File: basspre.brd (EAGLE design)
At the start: 41.3 x 28.7 mm, 27 parts, among them U1 LM4250, U101 TLE2426IDR, U103 LM4250

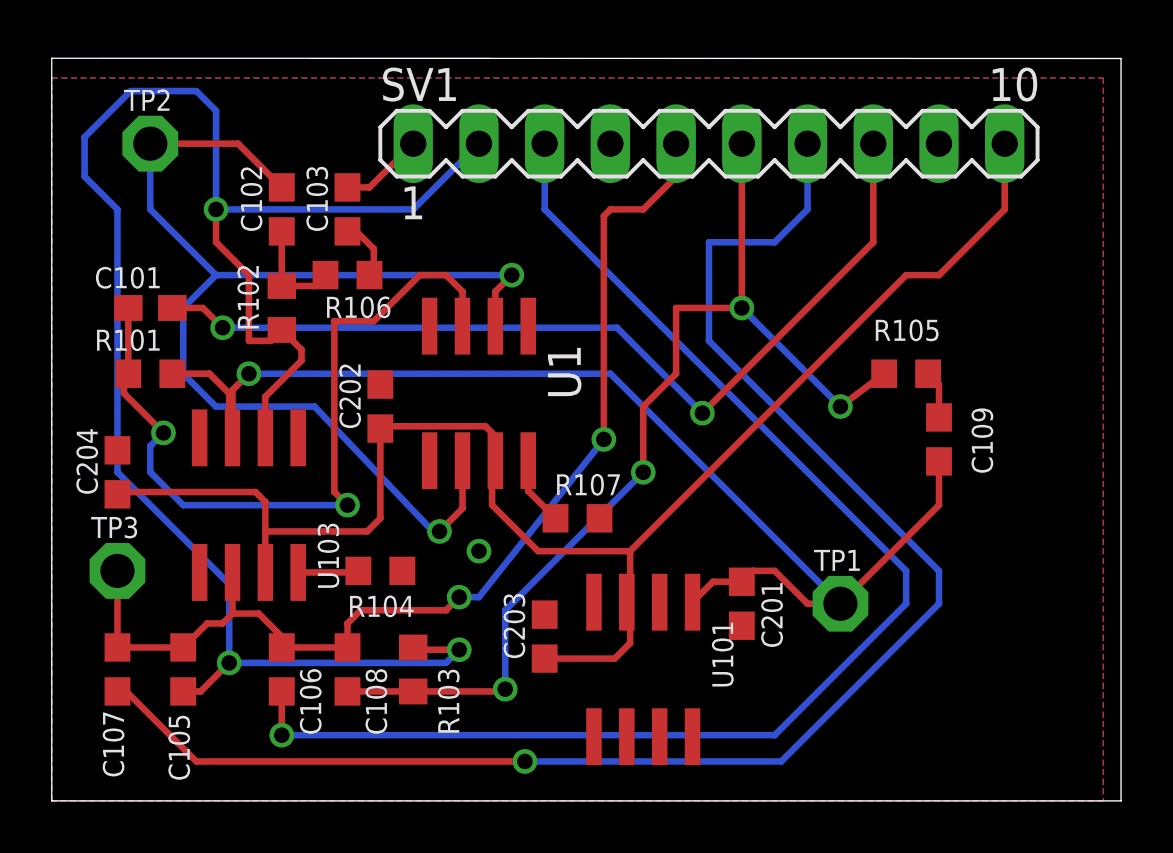
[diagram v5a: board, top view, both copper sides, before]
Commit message: changed bypass caps to 0805.
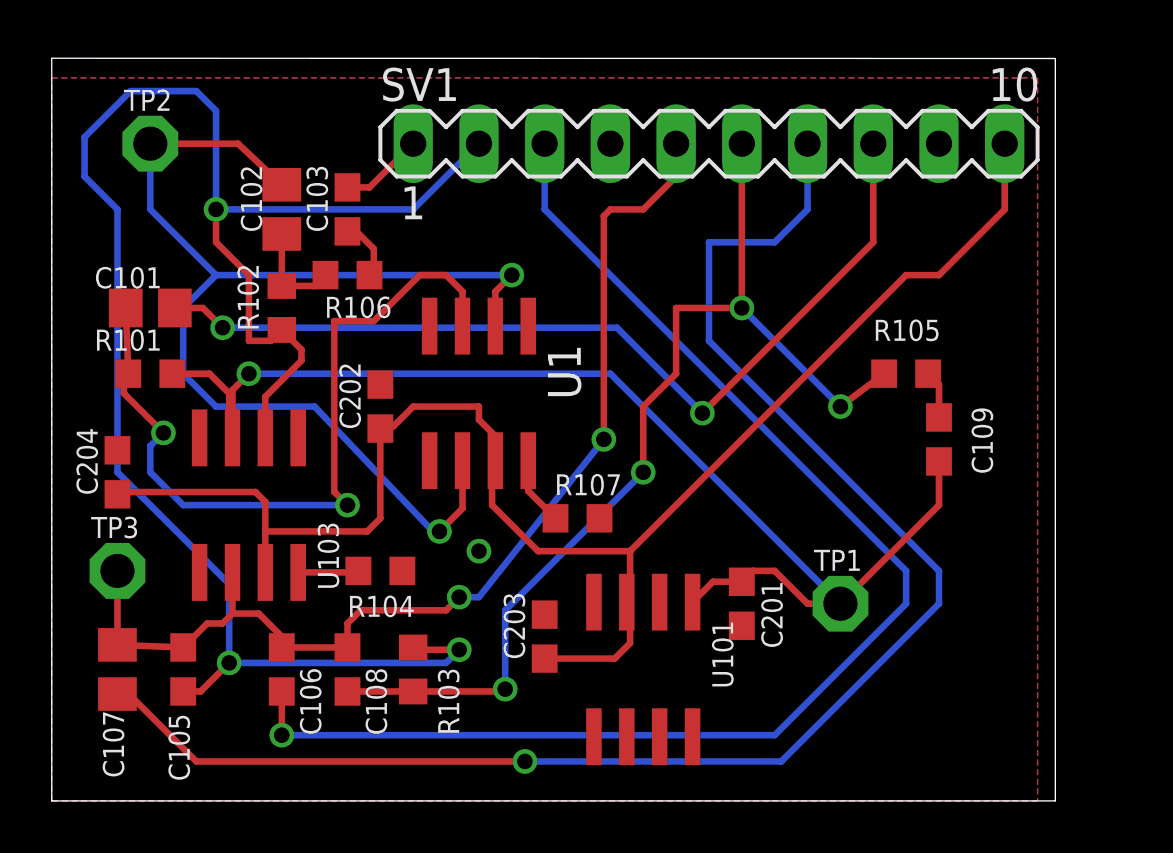
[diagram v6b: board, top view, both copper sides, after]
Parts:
- C101, C102, C107: device resistor:C0603 -> rcl:C0805
- C106: value 500pF -> 470pF
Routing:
- net V+: track 60.0 -> 60.9 mm
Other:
- board size 41.3 x 28.7 mm -> 38.8 x 28.7 mm
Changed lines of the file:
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@@
 <board>
 <plain>
-<wire x1="0" y1="0" x2="41.326" y2="0" width="0" layer="20"/>
-<wire x1="41.326" y1="0" x2="41.326" y2="28.692" width="0" layer="20"/>
-<wire x1="41.326" y1="28.692" x2="0" y2="28.702" width="0" layer="20"/>
+<wire x1="0" y1="0" x2="38.786" y2="0" width="0" layer="20"/>
+<wire x1="38.786" y1="0" x2="38.786" y2="28.692" width="0" layer="20"/>
+<wire x1="38.786" y1="28.692" x2="0" y2="28.702" width="0" layer="20"/>
 <wire x1="0" y1="28.702" x2="0" y2="0" width="0" layer="20"/>
 <text x="35.56" y="17.78" size="1.6764" layer="22" font="vector" rot="MR0">BASSPRE-MM2
@@
 <attribute name="VALUE" x="11.811" y="6.858" size="1.27" layer="27"/>
 </element>
-<element name="C101" library="resistor" package="C0603" value="1uF" x="3.81" y="19.05" smashed="yes">
+<element name="C101" library="rcl" package="C0805" value="1uF" x="3.81" y="19.05" smashed="yes">
 <attribute name="NAME" x="1.651" y="19.812" size="0.8128" layer="25"/>
 <attribute name="VALUE" x="2.921" y="17.018" size="1.27" layer="27"/>
@@
 <attribute name="VALUE" x="9.398" y="5.969" size="1.27" layer="27" rot="R270"/>
 </element>
-<element name="C102" library="resistor" package="C0603" value="1uF" x="8.89" y="22.86" smashed="yes" rot="R90">
+<element name="C102" library="rcl" package="C0805" value="1uF" x="8.89" y="22.86" smashed="yes" rot="R90">
 <attribute name="NAME" x="8.128" y="21.971" size="0.8128" layer="25" rot="R90"/>
 <attribute name="VALUE" x="10.922" y="21.971" size="1.27" layer="27" rot="R90"/>
@@
 <attribute name="VALUE" x="9.398" y="23.749" size="1.27" layer="27" rot="R270"/>
 </element>
-<element name="C106" library="resistor" package="C0603" value="500pF" x="8.89" y="5.08" smashed="yes" rot="R90">
+<element name="C106" library="resistor" package="C0603" value="470pF" x="8.89" y="5.08" smashed="yes" rot="R90">
 <attribute name="NAME" x="10.414" y="2.54" size="0.8128" layer="25" rot="R90"/>
 <attribute name="VALUE" x="10.922" y="4.191" size="1.27" layer="27" rot="R90"/>
 </element>
-<element name="C107" library="resistor" package="C0603" value="1uF" x="2.54" y="5.08" smashed="yes" rot="R90">
+<element name="C107" library="rcl" package="C0805" value="1uF" x="2.54" y="5.08" smashed="yes" rot="R90">
 <attribute name="NAME" x="2.794" y="0.889" size="0.8128" layer="25" rot="R90"/>
 <attribute name="VALUE" x="4.572" y="4.191" size="1.27" layer="27" rot="R90"/>
@@
 <vertex x="0" y="0"/>
 <vertex x="0" y="27.94"/>
-<vertex x="40.64" y="27.94"/>
-<vertex x="40.64" y="0"/>
+<vertex x="38.1" y="27.94"/>
+<vertex x="38.1" y="0"/>
 </polygon>
 <polygon width="0.4064" layer="1">
 <vertex x="0" y="27.94"/>
-<vertex x="40.64" y="27.94"/>
-<vertex x="40.64" y="0"/>
+<vertex x="38.1" y="27.94"/>
+<vertex x="38.1" y="0"/>
 <vertex x="0" y="0"/>
 </polygon>
@@
 <wire x1="18.796" y1="9.652" x2="17.018" y2="11.43" width="0.254" layer="1"/>
 <wire x1="17.018" y1="11.43" x2="17.018" y2="13.148" width="0.254" layer="1"/>
-<wire x1="17.145" y1="14.097" x2="16.764" y2="14.478" width="0.254" layer="1"/>
-<wire x1="16.764" y1="14.478" x2="12.788" y2="14.478" width="0.254" layer="1"/>
+<wire x1="17.145" y1="14.097" x2="16.51" y2="14.732" width="0.254" layer="1"/>
 <wire x1="12.788" y1="14.478" x2="12.7" y2="14.39" width="0.254" layer="1"/>
 <wire x1="8.255" y1="8.83" x2="8.255" y2="10.414" width="0.254" layer="1"/>
@@
 <wire x1="17.145" y1="14.097" x2="17.145" y2="13.148" width="0.254" layer="1"/>
 <wire x1="17.145" y1="13.148" x2="17.018" y2="13.148" width="0.254" layer="1"/>
+<wire x1="12.788" y1="14.478" x2="13.208" y2="14.478" width="0.254" layer="1"/>
+<wire x1="13.208" y1="14.478" x2="13.97" y2="15.24" width="0.254" layer="1"/>
+<wire x1="13.97" y1="15.24" x2="16.51" y2="15.24" width="0.254" layer="1"/>
+<wire x1="16.51" y1="15.24" x2="16.51" y2="14.732" width="0.254" layer="1"/>
 </signal>
 <signal name="N$2">
@@
 <contactref element="TP2" pad="TP"/>
 <wire x1="3.81" y1="25.4" x2="7.2" y2="25.4" width="0.254" layer="1"/>
-<wire x1="7.2" y1="25.4" x2="8.89" y2="23.71" width="0.254" layer="1"/>
+<wire x1="7.2" y1="25.4" x2="8.89" y2="23.81" width="0.254" layer="1"/>
 <wire x1="17.145" y1="19.685" x2="17.78" y2="20.32" width="0.254" layer="1"/>
 <via x="17.78" y="20.32" extent="1-16" drill="0.6" shape="square"/>
@@
 <contactref element="C101" pad="1"/>
 <contactref element="R101" pad="1"/>
-<wire x1="2.96" y1="19.05" x2="2.96" y2="16.51" width="0.254" layer="1"/>
+<wire x1="2.86" y1="19.05" x2="2.96" y2="16.51" width="0.254" layer="1"/>
 <wire x1="15.875" y1="19.685" x2="15.24" y2="20.32" width="0.254" layer="1"/>
 <wire x1="10.922" y1="18.542" x2="10.922" y2="11.938" width="0.254" layer="1"/>
@@
 <signal name="INPUT">
 <contactref element="C101" pad="2"/>
-<wire x1="4.66" y1="19.05" x2="5.842" y2="19.05" width="0.254" layer="1"/>
+<wire x1="4.76" y1="19.05" x2="5.842" y2="19.05" width="0.254" layer="1"/>
 <wire x1="5.842" y1="19.05" x2="6.604" y2="18.288" width="0.254" layer="1"/>
 <via x="6.604" y="18.288" extent="1-16" drill="0.6" shape="square"/>
@@
 <contactref element="TP3" pad="TP"/>
 <wire x1="8.89" y1="5.93" x2="11.43" y2="5.93" width="0.254" layer="1"/>
-<wire x1="2.54" y1="5.93" x2="5.08" y2="5.93" width="0.254" layer="1"/>
-<wire x1="2.54" y1="5.93" x2="2.54" y2="8.89" width="0.254" layer="1"/>
+<wire x1="2.54" y1="6.03" x2="5.08" y2="5.93" width="0.254" layer="1"/>
+<wire x1="2.54" y1="6.03" x2="2.54" y2="8.89" width="0.254" layer="1"/>
 <wire x1="6.985" y1="8.83" x2="6.985" y2="7.239" width="0.254" layer="1"/>
 <wire x1="6.985" y1="7.239" x2="6.604" y2="6.858" width="0.254" layer="1"/>
@@
 <contactref element="C102" pad="1"/>
 <contactref element="R102" pad="2"/>
-<wire x1="8.89" y1="22.01" x2="8.89" y2="19.9" width="0.254" layer="1"/>
+<wire x1="8.89" y1="21.91" x2="8.89" y2="19.9" width="0.254" layer="1"/>
 <contactref element="R106" pad="1"/>
 <wire x1="8.89" y1="19.9" x2="10.16" y2="19.9" width="0.254" layer="1"/>
@@
 <signal name="OUTPUT">
 <contactref element="C107" pad="1"/>
-<wire x1="2.54" y1="4.23" x2="2.882" y2="4.23" width="0.254" layer="1"/>
+<wire x1="2.54" y1="4.13" x2="2.882" y2="4.23" width="0.254" layer="1"/>
 <wire x1="2.882" y1="4.23" x2="5.588" y2="1.524" width="0.254" layer="1"/>
 <wire x1="5.588" y1="1.524" x2="18.288" y2="1.524" width="0.254" layer="1"/>

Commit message: added mouser order
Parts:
- C109: device resistor:C0603 -> rcl:C0805
- moved C109 1.27 mm to (34.3, 12.7)
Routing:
- net VGND: track 47.4 -> 46.0 mm
- net N$4: track 1.86 -> 3.03 mm
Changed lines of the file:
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@@
 <attribute name="VALUE" x="32.131" y="14.478" size="1.27" layer="27"/>
 </element>
-<element name="C109" library="resistor" package="C0603" value="10uF" x="34.29" y="13.97" smashed="yes" rot="R270">
-<attribute name="NAME" x="35.56" y="15.24" size="0.8128" layer="25" rot="R270"/>
-<attribute name="VALUE" x="32.258" y="14.859" size="1.27" layer="27" rot="R270"/>
+<element name="C109" library="rcl" package="C0805" value="10uF" x="34.29" y="12.7" smashed="yes" rot="R270">
+<attribute name="NAME" x="35.56" y="13.97" size="0.8128" layer="25" rot="R270"/>
+<attribute name="VALUE" x="32.258" y="13.589" size="1.27" layer="27" rot="R270"/>
 </element>
 <element name="R106" library="resistor" package="R0603" value="100K" x="11.43" y="20.32" smashed="yes">
@@
 <wire x1="21.59" y1="16.51" x2="30.48" y2="7.62" width="0.254" layer="16"/>
 <contactref element="C109" pad="2"/>
-<wire x1="34.29" y1="13.12" x2="34.29" y2="11.43" width="0.254" layer="1"/>
+<wire x1="34.29" y1="11.75" x2="34.29" y2="11.43" width="0.254" layer="1"/>
 <wire x1="34.29" y1="11.43" x2="30.48" y2="7.62" width="0.254" layer="1"/>
 </signal>
@@
 <contactref element="C109" pad="1"/>
 <contactref element="R105" pad="2"/>
-<wire x1="34.29" y1="14.82" x2="34.29" y2="16.09" width="0.254" layer="1"/>
+<wire x1="34.29" y1="13.65" x2="34.29" y2="16.09" width="0.254" layer="1"/>
 <wire x1="34.29" y1="16.09" x2="33.87" y2="16.51" width="0.254" layer="1"/>
 </signal>
